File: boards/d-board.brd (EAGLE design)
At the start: 45.7 x 89 mm, 32 parts, among them J1 AMP FCI 10103594-0001LF, U1 ESP-WROOM-32, U2 CP2104, U3 SP0503BAHT

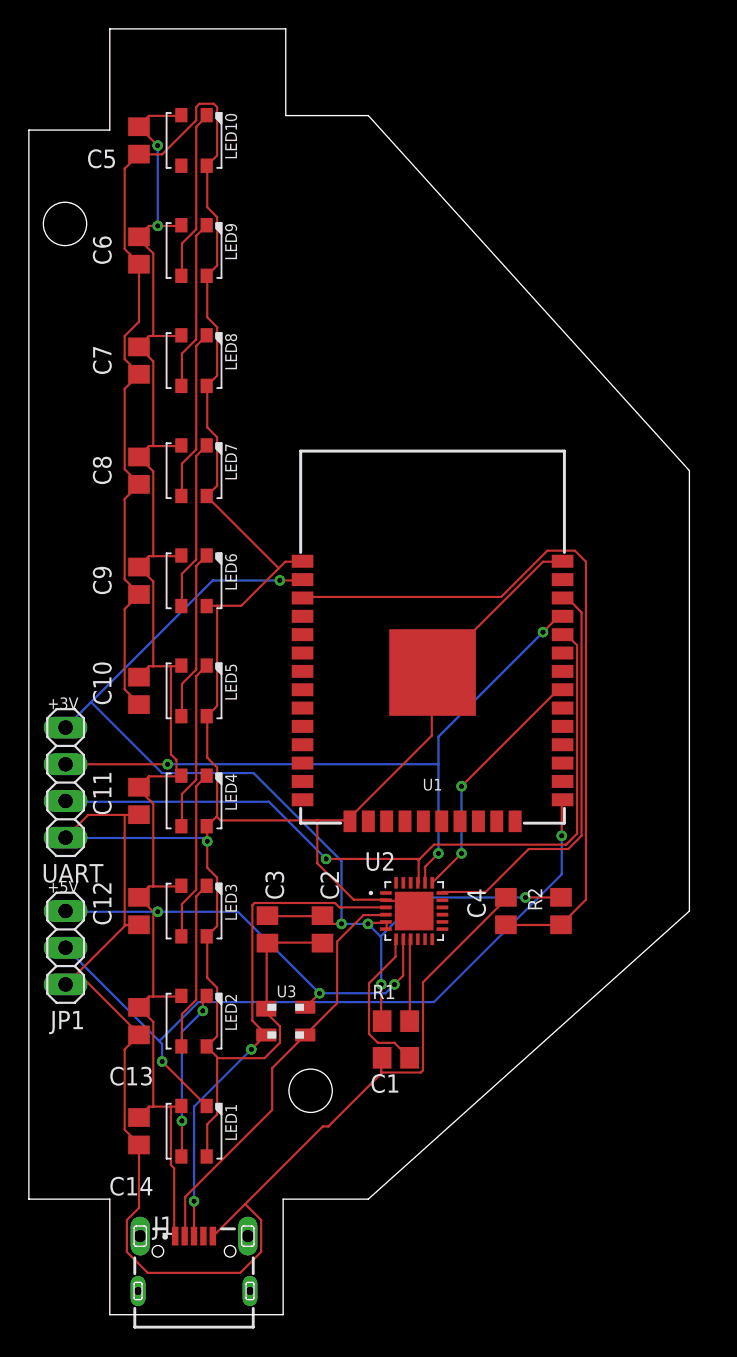
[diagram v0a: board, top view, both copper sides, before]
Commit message: Update board to rev.2
Fixes CP2104 REGIN not connected to +5V.

Replaces the mis-pinned 3535 neopixel with the 5050 part that is correct instead.
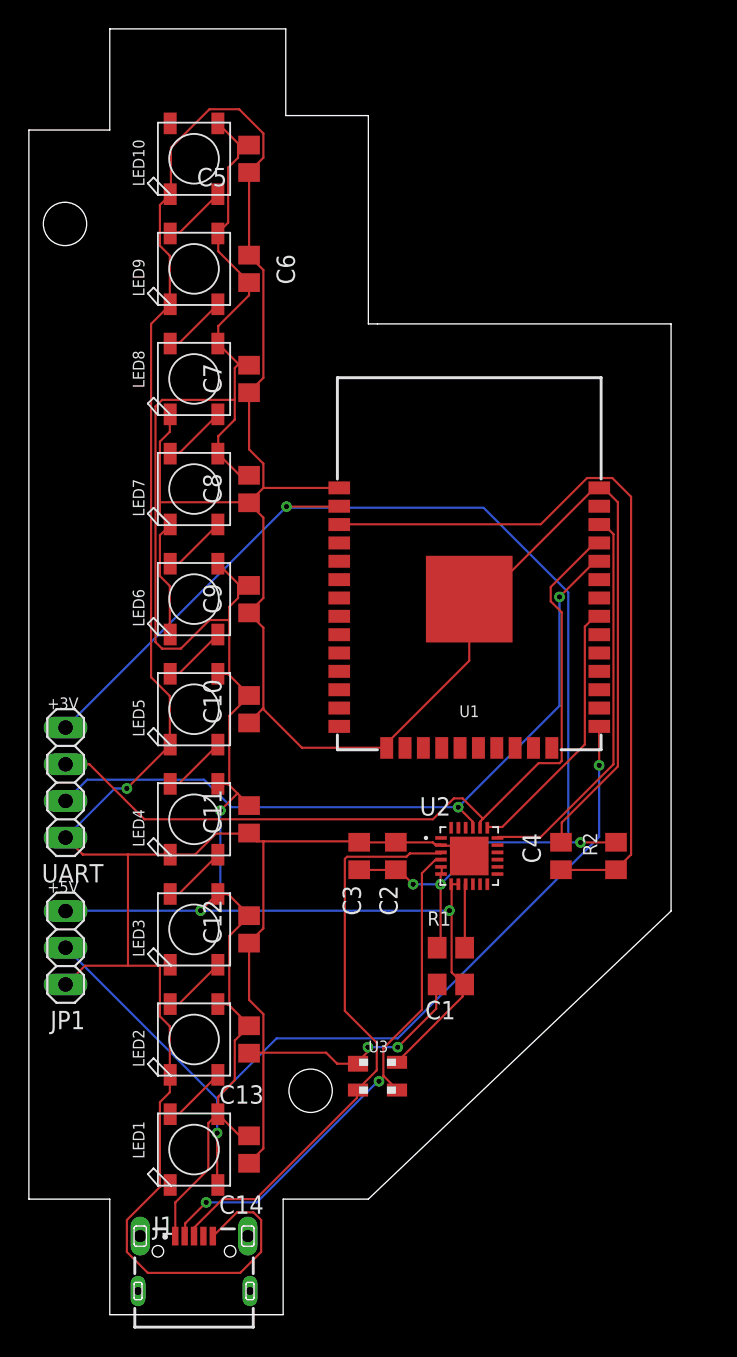
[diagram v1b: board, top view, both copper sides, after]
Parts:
- LED1, LED10, LED2, LED3, LED4, LED5, LED6, LED7, LED8, LED9: value WS2812B3535 -> WS2812B5050; device adafruit:LED3535 -> adafruit:WS2812B
- moved C3 8.13 mm to (22.9, 31.8), turned to 90 degrees
- moved C10 7.73 mm to (15.2, 41.9)
- moved C11 7.73 mm to (15.2, 34.3)
- moved C7 7.73 mm to (15.2, 64.8)
- moved C8 7.73 mm to (15.2, 57.1)
- moved C12 7.73 mm to (15.2, 26.7)
- moved C13 7.73 mm to (15.2, 19.1)
- moved C14 7.73 mm to (15.2, 11.4)
- moved C5 7.73 mm to (15.2, 80.0)
- moved C6 7.73 mm to (15.2, 72.4), turned to 90 degrees
- moved C9 7.73 mm to (15.2, 49.5)
- moved U3 7.41 mm to (24.1, 16.5)
- moved C2 7.18 mm to (25.4, 31.8), turned to 90 degrees
- moved C1 6.35 mm to (29.2, 22.9)
- moved R1 6.35 mm to (29.2, 25.4)
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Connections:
- removed net N$15: C1.2, U2.7
- net +5V: now also C1.2, LED1.1-VDD, LED10.1-VDD, LED2.1-VDD, LED3.1-VDD, LED4.1-VDD, LED5.1-VDD, LED6.1-VDD, LED7.1-VDD, LED8.1-VDD, LED9.1-VDD, U2.7; no longer LED1.2, LED10.2, LED2.2, LED3.2, LED4.2, LED5.2, LED6.2, LED7.2, LED8.2, LED9.2
- net GND: now also LED1.3-GND, LED10.3-GND, LED2.3-GND, LED3.3-GND, LED4.3-GND, LED5.3-GND, LED6.3-GND, LED7.3-GND, LED8.3-GND, LED9.3-GND; no longer LED1.4, LED10.4, LED2.4, LED3.4, LED4.4, LED5.4, LED6.4, LED7.4, LED8.4, LED9.4
- net N$1: now also LED1.4-DIN; no longer LED1.1
- net N$12: now also LED4.2-DOUT, LED5.4-DIN; no longer LED4.3, LED5.1
- net N$16: now also LED5.2-DOUT, LED6.4-DIN; no longer LED5.3, LED6.1
- net N$17: now also LED6.2-DOUT, LED7.4-DIN; no longer LED6.3, LED7.1
- net N$18: now also LED7.2-DOUT, LED8.4-DIN; no longer LED7.3, LED8.1
- net N$19: now also LED8.2-DOUT, LED9.4-DIN; no longer LED8.3, LED9.1
- net N$20: now also LED10.4-DIN, LED9.2-DOUT; no longer LED10.1, LED9.3
- net N$21: now also LED1.2-DOUT, LED2.4-DIN; no longer LED1.3, LED2.1
- net N$4: now also LED2.2-DOUT, LED3.4-DIN; no longer LED2.3, LED3.1
- net N$8: now also LED3.2-DOUT, LED4.4-DIN; no longer LED3.3, LED4.1
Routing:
- net +5V: track 139.1 -> 165.3 mm, vias 5 -> 3
- net GND: track 297.3 -> 319.7 mm, vias 1 -> 3
- net VDD: track 76.7 -> 89.7 mm, vias 5 -> 4
- net N$15: track 10.8 -> 0.00 mm
- net N$1: track 52.8 -> 62.4 mm
- net N$7: track 28.9 -> 37.1 mm, vias 0 -> 2
- net N$2: track 48.3 -> 56.4 mm, vias 3 -> 0
- net N$20: track 11.9 -> 4.44 mm
- net N$18: track 11.8 -> 4.44 mm
- net N$4: track 11.8 -> 4.44 mm
- net N$21: track 11.8 -> 4.44 mm, vias 2 -> 0
- net N$8: track 11.8 -> 4.44 mm
- net N$12: track 11.8 -> 4.44 mm
- net N$17: track 11.8 -> 4.44 mm
- net N$19: track 11.8 -> 4.44 mm
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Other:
- board size 45.7 x 89 mm -> 44.5 x 89 mm
- board text added: "Neopixel Acrylic Lamp rev. 2 Copyright © 2020 Diego Elio Pettenò flameeyes.com/p/espacrylic Licensed under MIT"
- board text removed: "Neopixel Acrylic Lamp rev. 1 Copyright © 2020 Diego Elio Pettenò flameeyes.com/p/espacrylic Licensed under MIT"

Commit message: Replace the microUSB connector.
Instead of the Wurth part that seems to be harder to find, use a SnapEDA for an Amphenol 10103594-0001LF connector that appears easier to source.
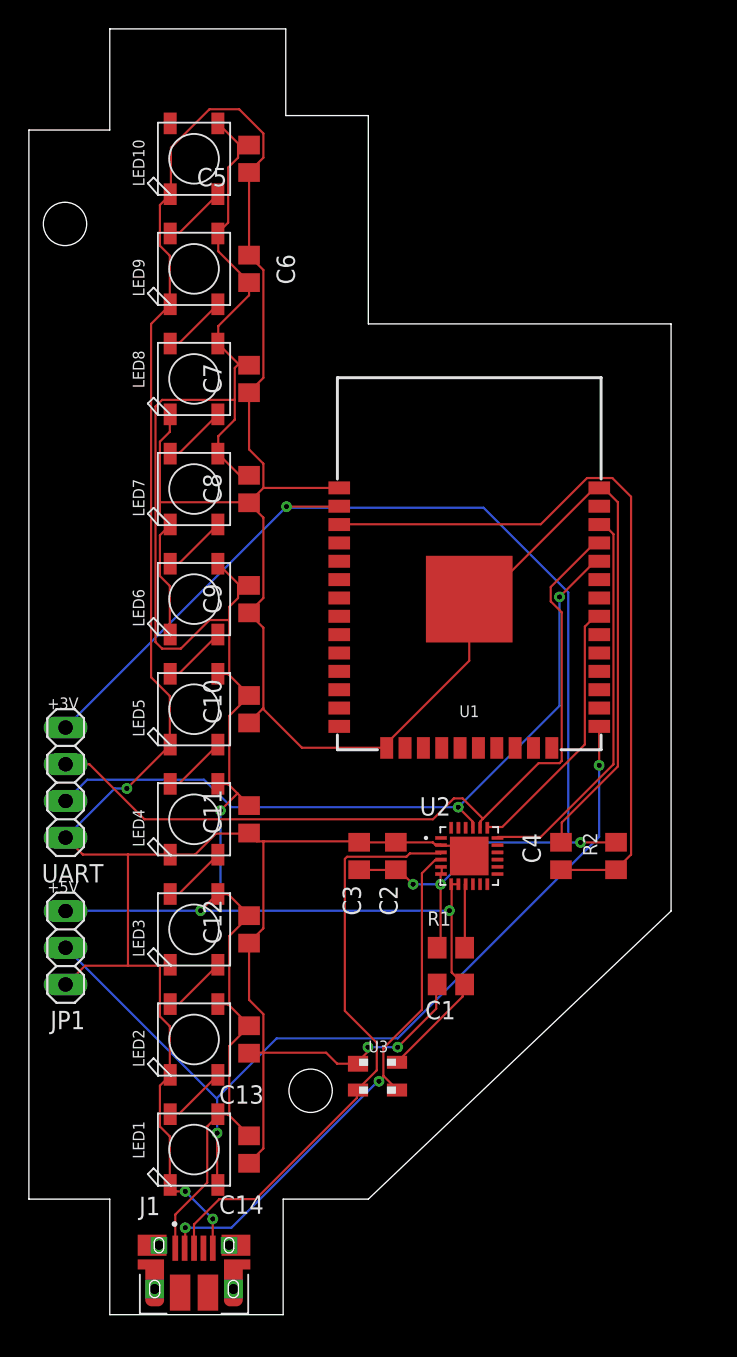
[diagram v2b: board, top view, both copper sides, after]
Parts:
- J1: value AMP FCI 10103594-0001LF -> 10103594-0001LF; device Wurth_Connectors_WR-USB:629105150521 -> 10103594-0001LF:FCI_10103594-0001LF
- moved J1 0.76 mm to (11.4, 1.78)
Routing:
- net GND: track 319.7 -> 302.7 mm, vias 3 -> 5
- net N$6: track 40.5 -> 41.5 mm
- net N$7: track 37.1 -> 37.7 mm
- net +5V: track 165.3 -> 165.9 mm
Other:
- outline, holes or cut-outs redrawn

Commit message: Make it possible to program the ESP32 via serial.
This includes RESET and BOOT pushbuttons to control a solder ESP32, and re-wires the RTS/DTR to control the boot mode of the board for compatibility with the esptool command line.
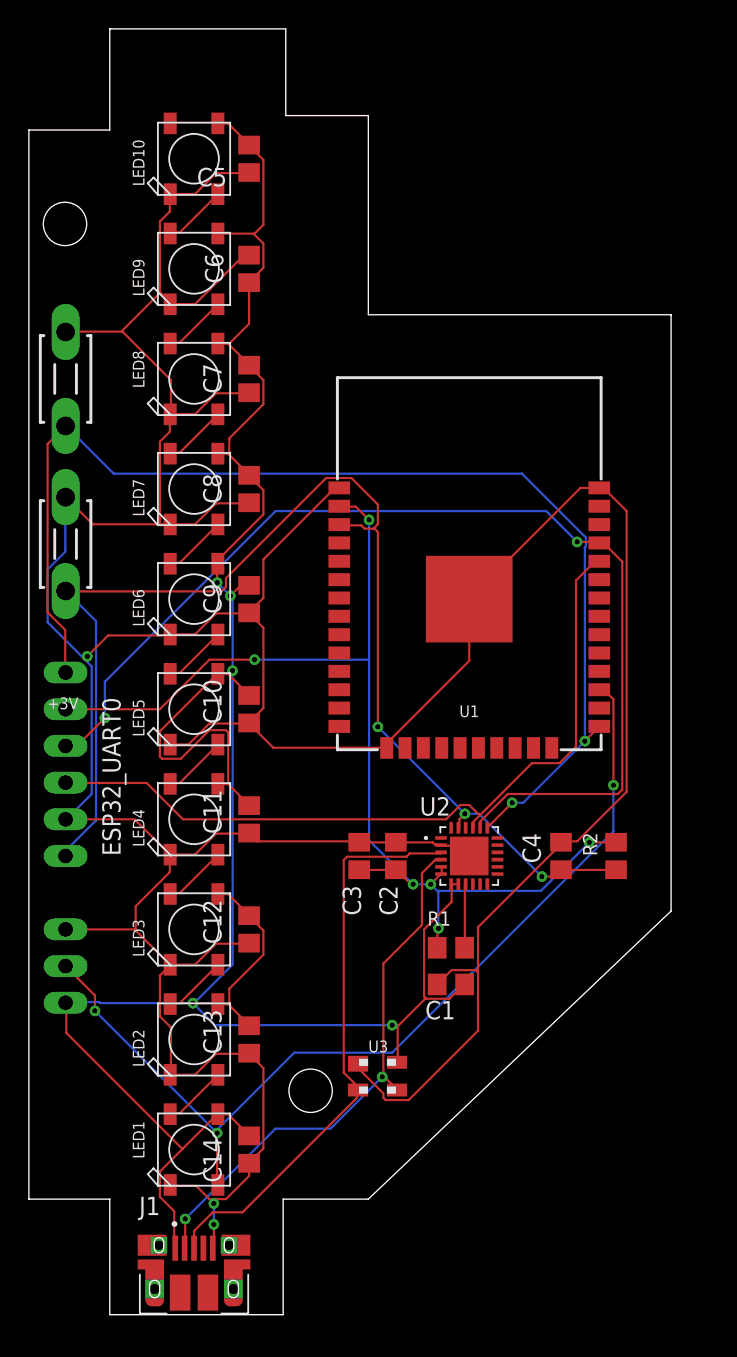
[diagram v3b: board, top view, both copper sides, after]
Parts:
- added BOOT, RESET: DTS-3, switch-tact:DTS-3
- JP1: value (none) -> PINHD-1X3/90; device pinhead:1X03 -> Connector:1X03/90
- UART: value PINHD-1X4 -> PINHD-1X6/90; device Connector:1X04 -> Connector:1X06/90
- moved UART 4.02 mm to (-1.27, 38.1), flipped to the bottom
- moved JP1 4.02 mm to (-1.27, 24.1), flipped to the bottom, turned to 270 degrees
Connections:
- removed net N$13: U1.31, U2.19
- removed net N$14: U1.36, U2.18
- removed net N$2: U1.35, U2.20, UART.2
- removed net N$3: U1.34, U2.21, UART.3
- removed net N$9: C4.1, R2.1, U1.3
- new net ESP32_CTS: BOOT.2, U1.25, U2.19, UART.1
- new net ESP32_RTS: C4.1, R2.1, RESET.2, U1.3, U2.23, UART.6
- new net FROM_ESP: U1.35, U2.20, UART.3
- new net TO_ESP: U1.34, U2.21, UART.4
- net GND: now also BOOT.1, RESET.1, UART.5; no longer UART.4
- net N$1: now also U1.27; no longer U1.25
- net VDD: now also UART.2; no longer UART.1
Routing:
- net ESP32_RTS: track 0.00 -> 86.4 mm, vias 0 -> 3
- net ESP32_CTS: track 0.00 -> 82.1 mm, vias 0 -> 2
- net FROM_ESP: track 0.00 -> 75.2 mm, vias 0 -> 2
- net N$2: track 56.4 -> 0.00 mm
- net TO_ESP: track 0.00 -> 53.8 mm
- net N$9: track 52.1 -> 0.00 mm
- net N$3: track 51.7 -> 0.00 mm, vias 2 -> 0
- net N$14: track 27.3 -> 0.00 mm
- net N$13: track 18.6 -> 0.00 mm
- net +5V: track 165.9 -> 182.4 mm, vias 3 -> 5
- net VDD: track 89.7 -> 76.7 mm, vias 4 -> 6
- net N$1: track 62.4 -> 66.2 mm, vias 2 -> 3
- net GND: track 302.7 -> 305.6 mm, vias 5 -> 3
- net N$6: track 41.5 -> 40.2 mm
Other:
- outline, holes or cut-outs redrawn
- board text added: "!BOOT +3V TXD RXD GND !RST"
- board text added: "ESP32_UART0"
- board text added: "GND PXL +5V"
- board text added: "Neopixel Acrylic Lamp rev. 3 Copyright © 2020 Diego Elio Pettenò flameeyes.com/p/espacrylic Licensed under MIT"
- board text removed: "+5V"
- board text removed: "Neopixel Acrylic Lamp rev. 2 Copyright © 2020 Diego Elio Pettenò flameeyes.com/p/espacrylic Licensed under MIT"

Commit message: Replace the CP2104 with a CP2102
The CP2104 is getting harder to source, the CP2102 is pretty much equivalent, but requires more components.
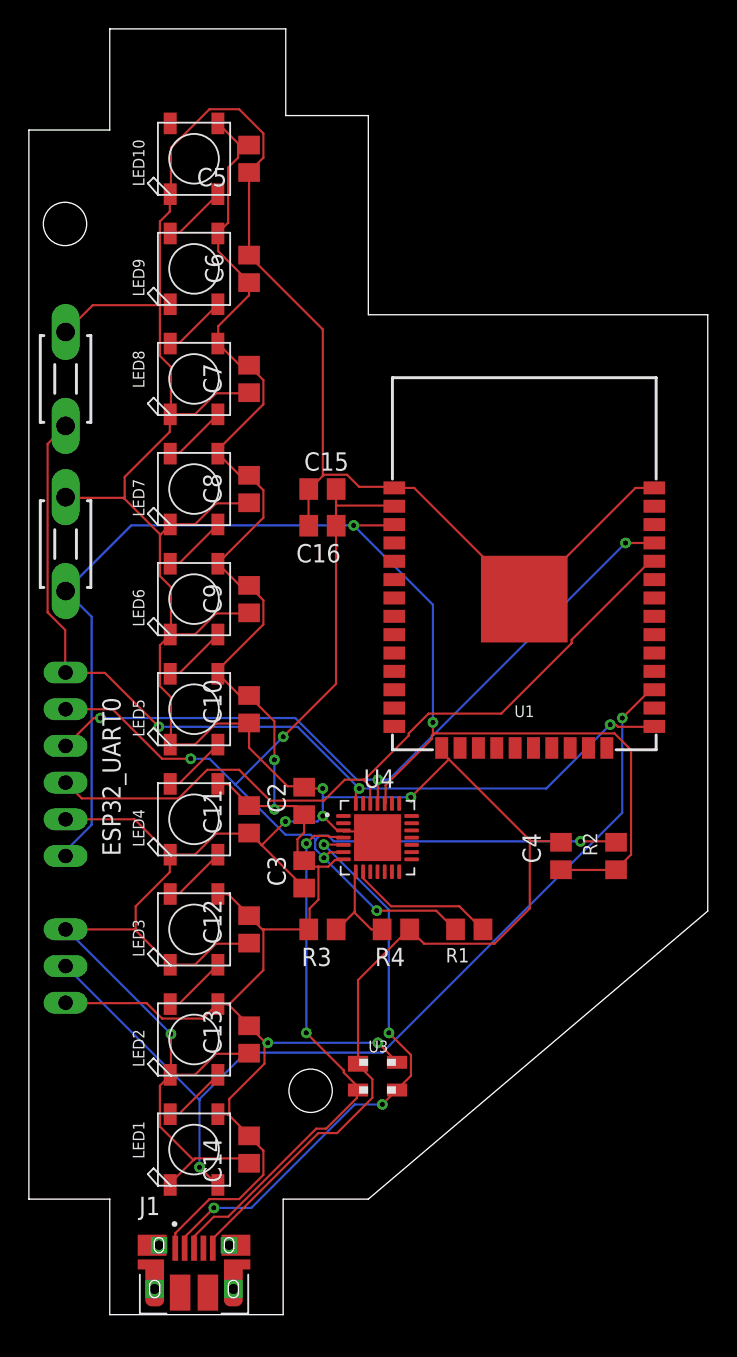
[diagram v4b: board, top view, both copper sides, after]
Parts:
- removed C1: 1uF, rcl:C0805
- removed U2: CP2104, CP2104:QFN50P400X400X80-25N
- added C15: 0.1uF, rcl:C0805
- added C16: 4.7uF, rcl:C0805
- added R3: 22.1k, rcl:R0805
- added R4: 47.5k, rcl:R0805
- added U4: CP2102N-A01-GQFN28, CP2102N-A01-GQFN28:QFN50P500X500X80-29N
- moved C2 7.41 mm to (19.1, 35.6)
- moved C3 4.02 mm to (19.1, 30.5), turned to 270 degrees
- moved U1 3.81 mm to (34.3, 49.5)
- moved R1 1.80 mm to (30.5, 26.7)
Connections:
- removed net ESP32_CTS: BOOT.2, U1.25, U2.19, UART.1
- removed net ESP32_RTS: C4.1, R2.1, RESET.2, U1.3, U2.23, UART.6
- removed net N$6: J1.3, U2.3, U3.2
- removed net N$7: J1.2, U2.4, U3.3
- removed net VDD: C2.1, C3.1, R1.1, R2.2, U1.2, U2.5, U2.6, UART.2
- new net 3V3: C15.1, C16.1, R1.1, R2.2, U1.2, U4.6, UART.2
- new net D+: J1.3, U3.2, U4.4
- new net D-: J1.2, U3.3, U4.5
- new net ESP32_BOOT: BOOT.2, U1.25, U4.28, UART.1
- new net ESP32_EN: C4.1, R2.1, RESET.2, U1.3, U4.24, UART.6
- new net N$3: R3.1, R4.2, U4.8
- net +5V: now also C2.1, C3.1, R3.2, U4.7; no longer C1.2, U2.7, U2.8
- net FROM_ESP: now also U4.25; no longer U2.20
- net GND: now also C15.2, C16.2, R4.1, U4.29, U4.3; no longer C1.1, U2.2, U2.25
- net N$5: now also U4.9; no longer U2.9
- net TO_ESP: now also U4.26; no longer U2.21
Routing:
- net ESP32_EN: track 0.00 -> 94.2 mm, vias 0 -> 2
- net ESP32_RTS: track 86.4 -> 0.00 mm, vias 3 -> 0
- net 3V3: track 0.00 -> 83.8 mm, vias 0 -> 5
- net ESP32_CTS: track 82.1 -> 0.00 mm, vias 2 -> 0
- net VDD: track 76.7 -> 0.00 mm, vias 6 -> 0
- net ESP32_BOOT: track 0.00 -> 65.2 mm, vias 0 -> 3
- net +5V: track 182.4 -> 140.9 mm, vias 5 -> 4
- net D-: track 0.00 -> 40.9 mm, vias 0 -> 4
- net N$6: track 40.2 -> 0.00 mm
- net N$7: track 38.1 -> 0.00 mm, vias 2 -> 0
- net D+: track 0.00 -> 38.1 mm, vias 0 -> 2
- net FROM_ESP: track 75.2 -> 51.8 mm, vias 2 -> 3
- net N$3: track 0.00 -> 7.04 mm
- net N$5: track 4.45 -> 10.2 mm
- net GND: track 305.6 -> 308.3 mm, vias 3 -> 5
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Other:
- board size 44.5 x 89 mm -> 47 x 89 mm
- board text removed: "+3V"

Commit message: Use net names instead of very long connections.
This allows an easier read of the diagram.
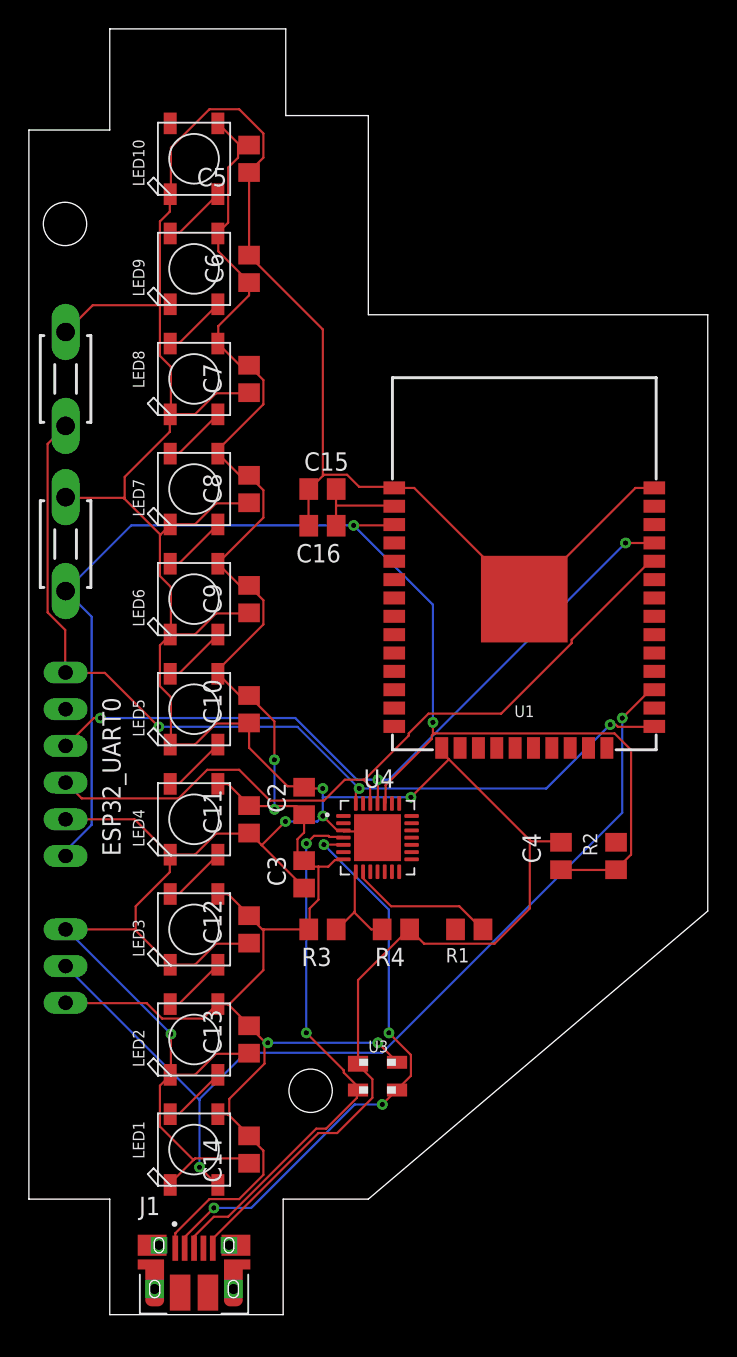
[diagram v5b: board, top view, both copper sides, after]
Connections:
- net ESP32_BOOT renamed ESP_BOOT
- net ESP32_EN renamed ESP_EN
- net FROM_ESP renamed ESP_TX
- net N$1 renamed NEOPIXEL_DATA
- net TO_ESP renamed ESP_RX
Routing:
- net 3V3: track 83.8 -> 6.60 mm, vias 5 -> 0
